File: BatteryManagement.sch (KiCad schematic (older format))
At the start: 20 parts, among them J401 Bootstrap, U401 AP9211, U402 MCP73213T-A6BI_MF

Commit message: Cleaning up some nets, adding input caps on power.
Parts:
- gave numbers to parts that had none: 9
- renumbered C401 to C201, C409 to C202, C410 to C203, D401 to D201, J401 to J201, R401 to R201, R405 to R202, R402 to R203, R406 to R204, U401 to U201, U402 to U202
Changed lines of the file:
@@
 $Descr A4 11693 8268
 encoding utf-8
-Sheet 3 3
+Sheet 2 3
 Title ""
 Date ""
@@
 P 2750 5100
 AR Path="/5DA95EB0/5DAAD200/5DC173E3" Ref="U?"  Part="1"
-AR Path="/5DC297AB/5DC173E3" Ref="U401"  Part="1"
-F 0 "U401" H 2750 5525 50  0000 C CNN
+AR Path="/5DC297AB/5DC173E3" Ref="U201"  Part="1"
+F 0 "U201" H 2750 5525 50  0000 C CNN
 F 1 "AP9211" H 2750 5434 50  0000 C CNN
 F 2 "libs:6-UDFN-Exposed-Pad" H 2750 4950 50  0001 C CNN
@@
 AR Path="/5DD0667E" Ref="C?"  Part="1"
 AR Path="/5DA95EB0/5DD0667E" Ref="C?"  Part="1"
-AR Path="/5DC297AB/5DD0667E" Ref="C401"  Part="1"
-F 0 "C401" H 2015 5196 50  0000 L CNN
+AR Path="/5DC297AB/5DD0667E" Ref="C201"  Part="1"
+F 0 "C201" H 2015 5196 50  0000 L CNN
 F 1 "100nF" H 2015 5105 50  0000 L CNN
 F 2 "Capacitors_SMD:C_0603" H 1938 5000 50  0001 C CNN
@@
 P 3650 5250
 AR Path="/5DE42ED8" Ref="R?"  Part="1"
-AR Path="/5DC297AB/5DE42ED8" Ref="R402"  Part="1"
-F 0 "R402" V 3550 5150 50  0000 C CNN
+AR Path="/5DC297AB/5DE42ED8" Ref="R203"  Part="1"
+F 0 "R203" V 3550 5150 50  0000 C CNN
 F 1 "2k7" V 3550 5350 50  0000 C CNN
 F 2 "Resistors_SMD:R_0603" V 3580 5250 50  0001 C CNN
@@
 P 1900 4650
 AR Path="/5DE426CE" Ref="R?"  Part="1"
-AR Path="/5DC297AB/5DE426CE" Ref="R401"  Part="1"
-F 0 "R401" V 1800 4550 50  0000 C CNN
+AR Path="/5DC297AB/5DE426CE" Ref="R201"  Part="1"
+F 0 "R201" V 1800 4550 50  0000 C CNN
 F 1 "470" V 1800 4750 50  0000 C CNN
 F 2 "Resistor_SMD:R_0603_1608Metric_Pad1.05x0.95mm_HandSolder" V 1830 4650 50  0001 C CNN
@@
 $EndComp
 $Comp
-L Connector_Generic:Conn_01x02 J401
+L Connector_Generic:Conn_01x02 J201
 U 1 1 5DE79FB0
 P 2800 5950
-F 0 "J401" V 2672 6030 50  0000 L CNN
+F 0 "J201" V 2672 6030 50  0000 L CNN
 F 1 "Bootstrap" V 2763 6030 50  0000 L CNN
 F 2 "Pin_Headers:Pin_Header_Straight_1x02_Pitch2.54mm" H 2800 5950 50  0001 C CNN
@@
 Batt-S1
 $Comp
-L dingo-hat:MCP73213T-A6BI_MF U402
+L dingo-hat:MCP73213T-A6BI_MF U202
 U 1 1 5DE8020F
 P 3300 3100
-F 0 "U402" H 3100 3500 60  0000 C CNN
+F 0 "U202" H 3100 3500 60  0000 C CNN
 F 1 "MCP73213T-A6BI_MF" H 2800 2700 60  0000 C CNN
 F 2 "libs:MCP73213T-A6BI" H 3850 2600 60  0001 C CNN
@@
 P 2150 3100
 AR Path="/5DE917F2" Ref="D?"  Part="1"
-AR Path="/5DC297AB/5DE917F2" Ref="D401"  Part="1"
-F 0 "D401" H 2142 2845 50  0000 C CNN
+AR Path="/5DC297AB/5DE917F2" Ref="D201"  Part="1"
+F 0 "D201" H 2142 2845 50  0000 C CNN
 F 1 "PWR" H 2142 2936 50  0000 C CNN
 F 2 "LED_SMD:LED_0603_1608Metric_Pad1.05x0.95mm_HandSolder" H 2150 3100 50  0001 C CNN
@@
 P 2550 3100
 AR Path="/5DE917FF" Ref="R?"  Part="1"
-AR Path="/5DC297AB/5DE917FF" Ref="R405"  Part="1"
-F 0 "R405" V 2450 3000 50  0000 C CNN
+AR Path="/5DC297AB/5DE917FF" Ref="R202"  Part="1"
+F 0 "R202" V 2450 3000 50  0000 C CNN
 F 1 "470" V 2450 3200 50  0000 C CNN
 F 2 "Resistors_SMD:R_0603" V 2480 3100 50  0001 C CNN
@@
 P 3300 3750
 AR Path="/5DE92439" Ref="#PWR?"  Part="1"
-AR Path="/5DC297AB/5DE92439" Ref="#PWR0411"  Part="1"
-F 0 "#PWR0411" H 3300 3500 50  0001 C CNN
+AR Path="/5DC297AB/5DE92439" Ref="#PWR0202"  Part="1"
+F 0 "#PWR0202" H 3300 3500 50  0001 C CNN
 F 1 "GND" H 3305 3577 50  0000 C CNN
 F 2 "" H 3300 3750 50  0001 C CNN
@@
 P 4000 3750
 AR Path="/5DE92A2E" Ref="#PWR?"  Part="1"
-AR Path="/5DC297AB/5DE92A2E" Ref="#PWR0413"  Part="1"
-F 0 "#PWR0413" H 4000 3500 50  0001 C CNN
+AR Path="/5DC297AB/5DE92A2E" Ref="#PWR0204"  Part="1"
+F 0 "#PWR0204" H 4000 3500 50  0001 C CNN
 F 1 "GND" H 4005 3577 50  0000 C CNN
 F 2 "" H 4000 3750 50  0001 C CNN
@@
 P 3650 5750
 AR Path="/5DE96FDF" Ref="#PWR?"  Part="1"
-AR Path="/5DC297AB/5DE96FDF" Ref="#PWR0412"  Part="1"
-F 0 "#PWR0412" H 3650 5500 50  0001 C CNN
+AR Path="/5DC297AB/5DE96FDF" Ref="#PWR0203"  Part="1"
+F 0 "#PWR0203" H 3650 5500 50  0001 C CNN
 F 1 "GND" H 3655 5577 50  0000 C CNN
 F 2 "" H 3650 5750 50  0001 C CNN
@@
 P 4250 3200
 AR Path="/5DE98E07" Ref="R?"  Part="1"
-AR Path="/5DC297AB/5DE98E07" Ref="R406"  Part="1"
-F 0 "R406" V 4150 3100 50  0000 C CNN
+AR Path="/5DC297AB/5DE98E07" Ref="R204"  Part="1"
+F 0 "R204" V 4150 3100 50  0000 C CNN
 F 1 "1k" V 4150 3300 50  0000 C CNN
 F 2 "Resistors_SMD:R_0603" V 4180 3200 50  0001 C CNN
@@
 AR Path="/5DEA4065" Ref="C?"  Part="1"
 AR Path="/5DA95EB0/5DEA4065" Ref="C?"  Part="1"
-AR Path="/5DC297AB/5DEA4065" Ref="C410"  Part="1"
-F 0 "C410" H 4715 3146 50  0000 L CNN
+AR Path="/5DC297AB/5DEA4065" Ref="C203"  Part="1"
+F 0 "C203" H 4715 3146 50  0000 L CNN
 F 1 "1uF" H 4715 3055 50  0000 L CNN
 F 2 "Capacitors_SMD:C_0603" H 4638 2950 50  0001 C CNN
@@
 AR Path="/5DEA4DE0" Ref="C?"  Part="1"
 AR Path="/5DA95EB0/5DEA4DE0" Ref="C?"  Part="1"
-AR Path="/5DC297AB/5DEA4DE0" Ref="C409"  Part="1"
-F 0 "C409" H 2065 3346 50  0000 L CNN
+AR Path="/5DC297AB/5DEA4DE0" Ref="C202"  Part="1"
+F 0 "C202" H 2065 3346 50  0000 L CNN
 F 1 "1uF" H 2065 3255 50  0000 L CNN
 F 2 "Capacitors_SMD:C_0603" H 1988 3150 50  0001 C CNN
@@
 P 1950 3750
 AR Path="/5DEA6514" Ref="#PWR?"  Part="1"
-AR Path="/5DC297AB/5DEA6514" Ref="#PWR0410"  Part="1"
-F 0 "#PWR0410" H 1950 3500 50  0001 C CNN
+AR Path="/5DC297AB/5DEA6514" Ref="#PWR0201"  Part="1"
+F 0 "#PWR0201" H 1950 3500 50  0001 C CNN
 F 1 "GND" H 1955 3577 50  0000 C CNN
 F 2 "" H 1950 3750 50  0001 C CNN
@@
 P 8750 4200
 AR Path="/5DEB7344" Ref="R?"  Part="1"
-AR Path="/5DC297AB/5DEB7344" Ref="R?"  Part="1"
-F 0 "R?" V 8650 4100 50  0000 C CNN
+AR Path="/5DC297AB/5DEB7344" Ref="R208"  Part="1"
+F 0 "R208" V 8650 4100 50  0000 C CNN
 F 1 "150" V 8650 4300 50  0000 C CNN
 F 2 "Resistors_SMD:R_0603" V 8680 4200 50  0001 C CNN
@@
 AR Path="/5DEB7927" Ref="C?"  Part="1"
 AR Path="/5DA95EB0/5DEB7927" Ref="C?"  Part="1"
-AR Path="/5DC297AB/5DEB7927" Ref="C?"  Part="1"
-F 0 "C?" H 6815 4796 50  0000 L CNN
+AR Path="/5DC297AB/5DEB7927" Ref="C205"  Part="1"
+F 0 "C205" H 6815 4796 50  0000 L CNN
 F 1 "1uF" H 6815 4705 50  0000 L CNN
 F 2 "Capacitors_SMD:C_0603" H 6738 4600 50  0001 C CNN
@@
 AR Path="/5DEB7D1E" Ref="C?"  Part="1"
 AR Path="/5DA95EB0/5DEB7D1E" Ref="C?"  Part="1"
-AR Path="/5DC297AB/5DEB7D1E" Ref="C?"  Part="1"
-F 0 "C?" H 6815 4396 50  0000 L CNN
+AR Path="/5DC297AB/5DEB7D1E" Ref="C204"  Part="1"
+F 0 "C204" H 6815 4396 50  0000 L CNN
 F 1 "1uF" H 6815 4305 50  0000 L CNN
 F 2 "Capacitors_SMD:C_0603" H 6738 4200 50  0001 C CNN
@@
 AR Path="/5DEB7E1B" Ref="C?"  Part="1"
 AR Path="/5DA95EB0/5DEB7E1B" Ref="C?"  Part="1"
-AR Path="/5DC297AB/5DEB7E1B" Ref="C?"  Part="1"
-F 0 "C?" H 8865 4696 50  0000 L CNN
+AR Path="/5DC297AB/5DEB7E1B" Ref="C207"  Part="1"
+F 0 "C207" H 8865 4696 50  0000 L CNN
 F 1 "1uF" H 8865 4605 50  0000 L CNN
 F 2 "Capacitors_SMD:C_0603" H 8788 4500 50  0001 C CNN
@@
 P 6350 4550
 AR Path="/5DEC307F" Ref="R?"  Part="1"
-AR Path="/5DC297AB/5DEC307F" Ref="R?"  Part="1"
-F 0 "R?" V 6250 4450 50  0000 C CNN
+AR Path="/5DC297AB/5DEC307F" Ref="R205"  Part="1"
+F 0 "R205" V 6250 4450 50  0000 C CNN
 F 1 "240" V 6250 4650 50  0000 C CNN
 F 2 "Resistors_SMD:R_0603" V 6280 4550 50  0001 C CNN
@@
 P 6350 5100
 AR Path="/5DEC3348" Ref="R?"  Part="1"
-AR Path="/5DC297AB/5DEC3348" Ref="R?"  Part="1"
-F 0 "R?" V 6250 5000 50  0000 C CNN
+AR Path="/5DC297AB/5DEC3348" Ref="R206"  Part="1"
+F 0 "R206" V 6250 5000 50  0000 C CNN
 F 1 "150" V 6250 5200 50  0000 C CNN
 F 2 "Resistors_SMD:R_0603" V 6280 5100 50  0001 C CNN
@@
 P 6700 3900
 AR Path="/5DEC1918" Ref="R?"  Part="1"
-AR Path="/5DC297AB/5DEC1918" Ref="R?"  Part="1"
-F 0 "R?" V 6600 3800 50  0000 C CNN
+AR Path="/5DC297AB/5DEC1918" Ref="R207"  Part="1"
+F 0 "R207" V 6600 3800 50  0000 C CNN
 F 1 "150" V 6600 4000 50  0000 C CNN
 F 2 "Resistors_SMD:R_0603" V 6630 3900 50  0001 C CNN
@@
 AR Path="/5DED63F8" Ref="C?"  Part="1"
 AR Path="/5DA95EB0/5DED63F8" Ref="C?"  Part="1"
-AR Path="/5DC297AB/5DED63F8" Ref="C?"  Part="1"
-F 0 "C?" H 6815 5546 50  0000 L CNN
+AR Path="/5DC297AB/5DED63F8" Ref="C206"  Part="1"
+F 0 "C206" H 6815 5546 50  0000 L CNN
 F 1 "1uF" H 6815 5455 50  0000 L CNN
 F 2 "Capacitors_SMD:C_0603" H 6738 5350 50  0001 C CNN
@@
 Batt-S1
 $Comp
-L dingo-hat:BQ29209DRBR U?
+L dingo-hat:BQ29209DRBR U203
 U 1 1 5DEDCDDA
 P 7650 4700
-F 0 "U?" H 7650 5537 60  0000 C CNN
+F 0 "U203" H 7650 5537 60  0000 C CNN
 F 1 "BQ29209DRBR" H 7650 5431 60  0000 C CNN
 F 2 "DRB8_1P6X2P4" H 7650 4700 60  0001 C CNN

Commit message: Changing net names on balance charger.
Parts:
- added C?: 1uF, Capacitors_SMD:C_0603, symbol Device:C
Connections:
- net Batt+: no longer R207.2, R208.1
- net Batt-: no longer C205.2, C206.2, C207.2, U203.5 (GND), U203.6 (*CB_EN), U203.9 (EPAD)
- net Batt-S1 renamed VC1
- new net VC0: C205.2, C206.2, C207.2, U203.5 (GND), U203.6 (*CB_EN), U203.9 (EPAD)
- new net VC2: R207.2, R208.1
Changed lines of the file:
@@
 $Descr A4 11693 8268
 encoding utf-8
-Sheet 2 3
+Sheet 3 3
 Title ""
 Date ""
@@
 	2800 5650 2800 5750
 Connection ~ 2850 5650
-Text Label 3650 4950 0    50   ~ 0
-Batt-S1
 $Comp
 L dingo-hat:MCP73213T-A6BI_MF U202
@@
 $EndComp
 Text Label 6700 3700 0    50   ~ 0
-Batt+
+VC2
 $Comp
 L Device:C C?
@@
 Batt-
 Text Label 6700 5850 0    50   ~ 0
-Batt-
+VC0
 Text Label 6100 4850 0    50   ~ 0
-Batt-S1
+VC1
 $Comp
 L dingo-hat:BQ29209DRBR U203
@@
 	1    0    0    -1
 $EndComp
-Text Label 6700 4950 0    50   ~ 0
-Batt-
 Wire Wire Line
 	6700 4900 6700 4950
@@
 Wire Notes Line
 	9650 2350 5750 2350
+Text Label 1900 6100 0    50   ~ 0
+VC0
+$Comp
+L Device:C C?
+U 1 1 5DC6B2DE
+P 1900 5900
+AR Path="/5DC6B2DE" Ref="C?"  Part="1"
+AR Path="/5DA95EB0/5DC6B2DE" Ref="C?"  Part="1"
+AR Path="/5DC297AB/5DC6B2DE" Ref="C?"  Part="1"
+F 0 "C?" H 2015 5946 50  0000 L CNN
+F 1 "1uF" H 2015 5855 50  0000 L CNN
+F 2 "Capacitors_SMD:C_0603" H 1938 5750 50  0001 C CNN
+F 3 "~" H 1900 5900 50  0001 C CNN
+F 4 "0603" H 1800 6000 50  0000 L TNN "Package"
+F 5 "CAP CER 1UF 25V X5R 0603" H 1900 5900 50  0001 C CNN "Description"
+F 6 "25V" H 1900 5850 50  0000 R TNN "Voltage Rating"
+F 7 "https://www.digikey.com.au/product-detail/en/yageo/CC0603KRX5R8BB105/311-1445-1-ND/2833751" H 1900 5900 50  0001 C CNN "Link"
+F 8 "Digi-Key" H 1900 5900 50  0001 C CNN "Supplier 1"
+F 9 "311-1445-1-ND" H 1900 5900 50  0001 C CNN "Supplier Part Number 1"
+F 10 "0.15000" H 1900 5900 50  0001 C CNN "Unit Cost A$"
+	1    1900 5900
+	1    0    0    -1
+$EndComp
+Text Label 6700 4950 0    50   ~ 0
+VC0
+Text Label 3650 4950 0    50   ~ 0
+VC1
 $EndSCHEMATC

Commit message: Self notes.
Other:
- note added: "Does this protection really do what I want when there's a separate balance and power plug?"
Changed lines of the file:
@@
 Text Label 3650 4950 0    50   ~ 0
 VC1
+Text Notes 250  5050 0    118  ~ 24
+Does this protection really do what I want when there's a separate balance and power plug?
 $EndSCHEMATC

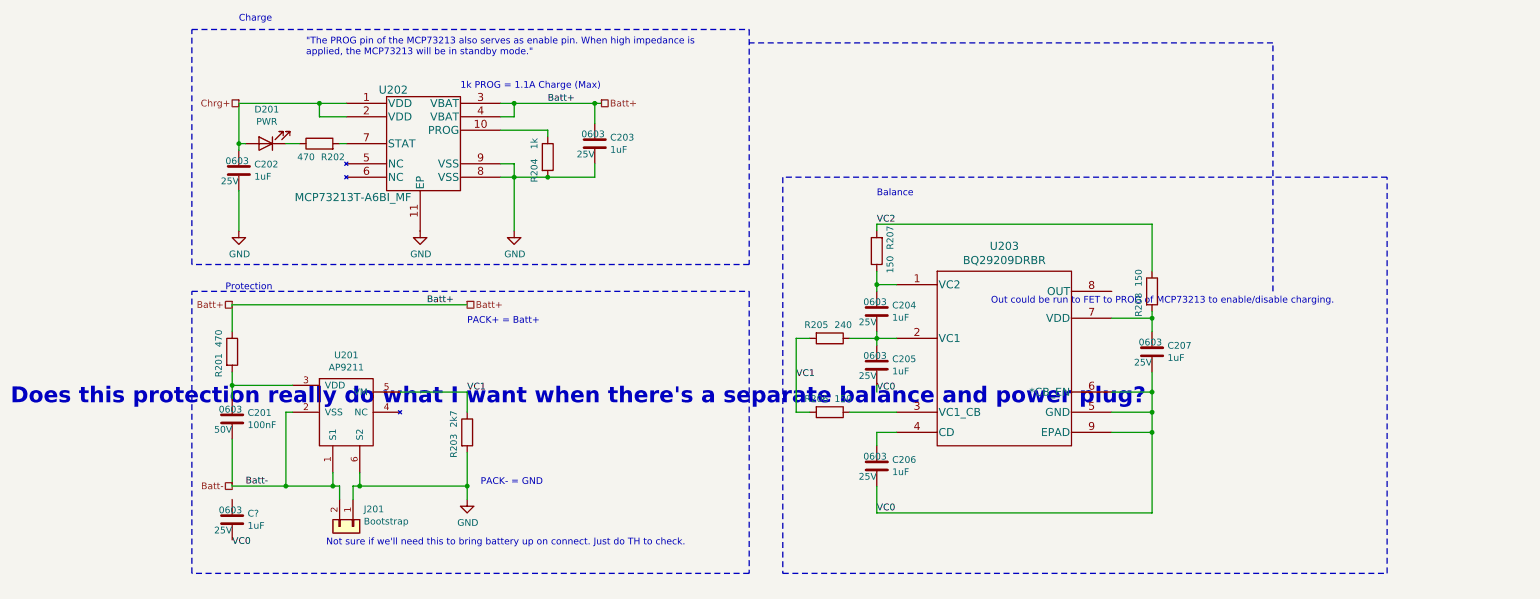
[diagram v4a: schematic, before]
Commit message: Power protection.
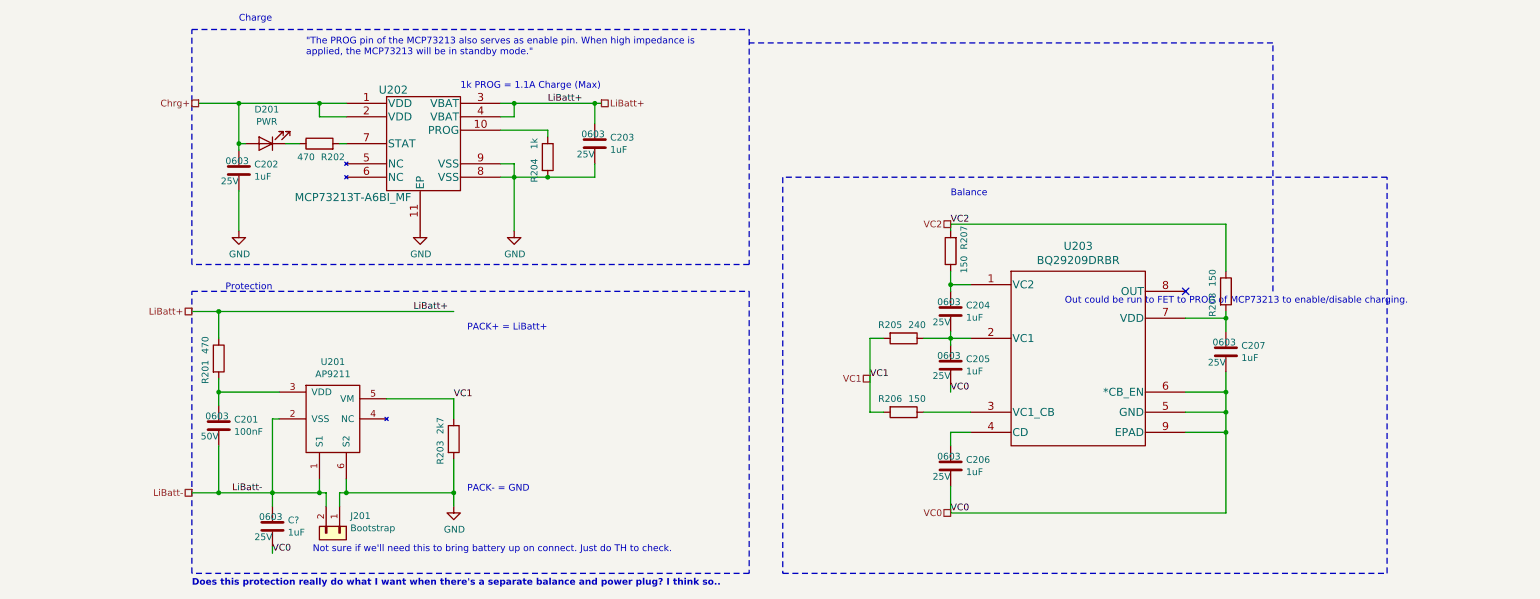
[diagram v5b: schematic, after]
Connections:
- net Batt- is gone; now on net LiBatt-: C201.2, J201.2 (Pin_2), U201.1 (S1), U201.2 (VSS)
- net VC0: now also C?.2
- net LiBatt-: now reaches C?.1
- net Batt+ renamed LiBatt+
- no-connect marks 0 -> 1
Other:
- note added: "Does this protection really do what I want when there's a separate balance and power plug? I think so.."
- note added: "PACK+ = LiBatt+"
- note removed: "Does this protection really do what I want when there's a separate balance and power plug?"
- note removed: "PACK+ = Batt+"
- moved on the sheet: C201, C204, C205, C206, C207, C?, J201, R201, R203, R205, R206, R207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

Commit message: Filling in some footprints, cleaning up schematic.
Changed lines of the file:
@@
 Text HLabel 1600 5700 0    50   UnSpc ~ 0
 LiBatt-
-Wire Wire Line
-	1800 4350 3550 4350
 $Comp
 L Device:R R?
@@
 Wire Wire Line
 	2550 2800 2750 2800
-Text HLabel 4650 2800 2    50   UnSpc ~ 0
-LiBatt+
 Wire Wire Line
 	3900 2900 4000 2900
@@
 Wire Wire Line
 	4600 2950 4600 2800
-Connection ~ 4600 2800
-Wire Wire Line
-	4600 2800 4650 2800
 Text Notes 3600 2700 0    50   ~ 0
 1k PROG = 1.1A Charge (Max)
@@
 Text Label 4250 2800 0    50   ~ 0
 LiBatt+
-Text Label 3250 4350 0    50   ~ 0
+Text Label 4250 4350 0    50   ~ 0
 LiBatt+
 Wire Wire Line
@@
 Connection ~ 1800 4350
 NoConn ~ 9000 4200
+Wire Wire Line
+	4600 2800 5400 2800
+Wire Wire Line
+	5400 2800 5400 4350
+Wire Wire Line
+	1800 4350 5400 4350
+Connection ~ 4600 2800
 $EndSCHEMATC

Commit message: Cleaning up schematics.
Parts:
- gave numbers to parts that had none: 1
- renumbered C203 to C204, C204 to C205, C205 to C206, C206 to C207, C207 to C208
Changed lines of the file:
@@
 AR Path="/5DEA4065" Ref="C?"  Part="1"
 AR Path="/5DA95EB0/5DEA4065" Ref="C?"  Part="1"
-AR Path="/5DC297AB/5DEA4065" Ref="C203"  Part="1"
-F 0 "C203" H 4715 3146 50  0000 L CNN
+AR Path="/5DC297AB/5DEA4065" Ref="C204"  Part="1"
+F 0 "C204" H 4715 3146 50  0000 L CNN
 F 1 "1uF" H 4715 3055 50  0000 L CNN
 F 2 "Capacitors_SMD:C_0603" H 4638 2950 50  0001 C CNN
@@
 AR Path="/5DEB7927" Ref="C?"  Part="1"
 AR Path="/5DA95EB0/5DEB7927" Ref="C?"  Part="1"
-AR Path="/5DC297AB/5DEB7927" Ref="C205"  Part="1"
-F 0 "C205" H 7365 4796 50  0000 L CNN
+AR Path="/5DC297AB/5DEB7927" Ref="C206"  Part="1"
+F 0 "C206" H 7365 4796 50  0000 L CNN
 F 1 "1uF" H 7365 4705 50  0000 L CNN
 F 2 "Capacitors_SMD:C_0603" H 7288 4600 50  0001 C CNN
@@
 AR Path="/5DEB7D1E" Ref="C?"  Part="1"
 AR Path="/5DA95EB0/5DEB7D1E" Ref="C?"  Part="1"
-AR Path="/5DC297AB/5DEB7D1E" Ref="C204"  Part="1"
-F 0 "C204" H 7365 4396 50  0000 L CNN
+AR Path="/5DC297AB/5DEB7D1E" Ref="C205"  Part="1"
+F 0 "C205" H 7365 4396 50  0000 L CNN
 F 1 "1uF" H 7365 4305 50  0000 L CNN
 F 2 "Capacitors_SMD:C_0603" H 7288 4200 50  0001 C CNN
@@
 AR Path="/5DEB7E1B" Ref="C?"  Part="1"
 AR Path="/5DA95EB0/5DEB7E1B" Ref="C?"  Part="1"
-AR Path="/5DC297AB/5DEB7E1B" Ref="C207"  Part="1"
-F 0 "C207" H 9415 4696 50  0000 L CNN
+AR Path="/5DC297AB/5DEB7E1B" Ref="C208"  Part="1"
+F 0 "C208" H 9415 4696 50  0000 L CNN
 F 1 "1uF" H 9415 4605 50  0000 L CNN
 F 2 "Capacitors_SMD:C_0603" H 9338 4500 50  0001 C CNN
@@
 AR Path="/5DED63F8" Ref="C?"  Part="1"
 AR Path="/5DA95EB0/5DED63F8" Ref="C?"  Part="1"
-AR Path="/5DC297AB/5DED63F8" Ref="C206"  Part="1"
-F 0 "C206" H 7365 5546 50  0000 L CNN
+AR Path="/5DC297AB/5DED63F8" Ref="C207"  Part="1"
+F 0 "C207" H 7365 5546 50  0000 L CNN
 F 1 "1uF" H 7365 5455 50  0000 L CNN
 F 2 "Capacitors_SMD:C_0603" H 7288 5350 50  0001 C CNN
@@
 AR Path="/5DC6B2DE" Ref="C?"  Part="1"
 AR Path="/5DA95EB0/5DC6B2DE" Ref="C?"  Part="1"
-AR Path="/5DC297AB/5DC6B2DE" Ref="C?"  Part="1"
-F 0 "C?" H 2315 5996 50  0000 L CNN
+AR Path="/5DC297AB/5DC6B2DE" Ref="C203"  Part="1"
+F 0 "C203" H 2315 5996 50  0000 L CNN
 F 1 "1uF" H 2315 5905 50  0000 L CNN
 F 2 "Capacitors_SMD:C_0603" H 2238 5800 50  0001 C CNN
